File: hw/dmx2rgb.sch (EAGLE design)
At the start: 4 parts, among them IC1 ATMEGA88-20A

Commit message: basic schematics added new parts to library
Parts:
- added C1, C2, C3, C6, C7, C8: 100n, dmx2rgb:C0805
- added C10, C9: 100µ, dmx2rgb:CPOL-EUE2.5-7
- added C4, C5: (no value), dmx2rgb:C0805
- added IC2: 7805, dmx2rgb:78LXX
- added PAD1, PAD10, PAD11, PAD12, PAD13, PAD14, PAD15, PAD16, PAD2, PAD3, PAD4, PAD5, PAD6, PAD7, PAD8, PAD9: (no value), dmx2rgb:PAD_THT_1.6
- added Q1: (no value), dmx2rgb:CRYSTAL49
- added R1: 10k, dmx2rgb:R0805
- added R2, R3: (no value), dmx2rgb:R0805
- added U$10, U$4, U$5, U$6, U$7, U$8, U$9: IRF7303, dmx2rgb:IRF7303
- added U$3: SN75176B, dmx2rgb:SN75176B
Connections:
- new net +12V: C8.1, C9.+, IC2.IN
- new net +5V: C1.2, C10.+, C2.2, C3.1, C6.2, C7.1, IC1.AREF, IC1.AVCC, IC1.VCC@1, IC1.VCC@2, IC2.OUT, JP1.2, R1.2, U$2.VDD, U$3.VCC
- new net GND: C1.1, C10.-, C2.1, C3.2, C4.2, C5.2, C6.1, C7.2, C8.2, C9.-, IC1.AGND, IC1.GND@1, IC1.GND@2, IC2.GND, JP1.10, JP1.3, JP1.4, JP1.6, JP1.8, U$1.S1, U$1.S2, U$10.S1, U$10.S2, U$2.EXTCLK, U$2.VSS, U$3.GND, U$4.S1, U$4.S2, U$5.S1, U$5.S2, U$6.S1, U$6.S2, U$7.S1, U$7.S2, U$8.S1, U$8.S2, U$9.S1, U$9.S2
- new net N$1: IC1.(PCI16/RXD)PD0, U$3.R
- new net N$10: IC1.(PCI5/SCK)PB5, JP1.7
- new net N$11: U$3.B
- new net N$12: U$3.A
- new net N$13: PAD3.P, U$4.D1A, U$4.D1B
- new net N$14: PAD4.P, U$4.D2A, U$4.D2B
- new net N$16: U$2.LED4, U$4.G2
- new net N$17: PAD5.P, U$5.D1A, U$5.D1B
- new net N$18: PAD6.P, U$5.D2A, U$5.D2B
- new net N$19: U$2.LED3, U$5.G1
- new net N$2: IC1.(PCI17/TXD)PD1, U$3.D
- new net N$20: U$2.LED2, U$5.G2
- new net N$21: PAD7.P, U$6.D1A, U$6.D1B
- new net N$22: PAD8.P, U$6.D2A, U$6.D2B
- new net N$23: U$2.LED1, U$6.G1
- new net N$24: U$2.LED0, U$6.G2
- new net N$25: PAD9.P, U$7.D1A, U$7.D1B
- new net N$26: PAD10.P, U$7.D2A, U$7.D2B
- new net N$29: PAD11.P, U$8.D1A, U$8.D1B
- new net N$3: IC1.(PCI18/INT0)PD2, U$3.RE
- new net N$30: PAD12.P, U$8.D2A, U$8.D2B
- new net N$33: PAD13.P, U$9.D1A, U$9.D1B
- new net N$34: PAD14.P, U$9.D2A, U$9.D2B
- new net N$37: PAD15.P, U$10.D1A, U$10.D1B
- new net N$38: PAD16.P, U$10.D2A, U$10.D2B
- new net N$4: IC1.(PCI19/INT1/OC2B)PD3, U$3.DE
- new net N$41: C4.1, IC1.PB6(XTAL1/TOSC1/PCI6), Q1.1
- new net N$42: C5.1, IC1.PB7(XTAL2/TOSC2/PCI7), Q1.2
- new net N$5: PAD1.P, U$1.D1A, U$1.D1B
- new net N$50: U$1.G1, U$2.LED7
- new net N$51: U$1.G2, U$2.LED6
- new net N$52: U$2.LED5, U$4.G1
- new net N$53: U$2.LED8, U$7.G1
- new net N$54: U$2.LED9, U$7.G2
- new net N$55: U$2.LED10, U$8.G1
- new net N$56: U$2.LED11, U$8.G2
- new net N$57: U$2.LED12, U$9.G1
- new net N$58: U$2.LED13, U$9.G2
- new net N$59: U$10.G1, U$2.LED14
- new net N$6: PAD2.P, U$1.D2A, U$1.D2B
- new net N$60: U$10.G2, U$2.LED15
- new net N$7: IC1.PC6(/RESET/PCI14), JP1.5, R1.1
- new net N$8: IC1.(PCI3/MOSI/OC2A)PB3, JP1.1
- new net N$9: IC1.(PCI4/MISO)PB4, JP1.9
- new net SCL: IC1.(PCI13/ADC5/SCL)PC5, U$2.SCL
- new net SDA: IC1.(PCI12/ADC4/SDA)PC4, U$2.SDA
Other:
- moved on the sheet: JP1, U$1, U$2

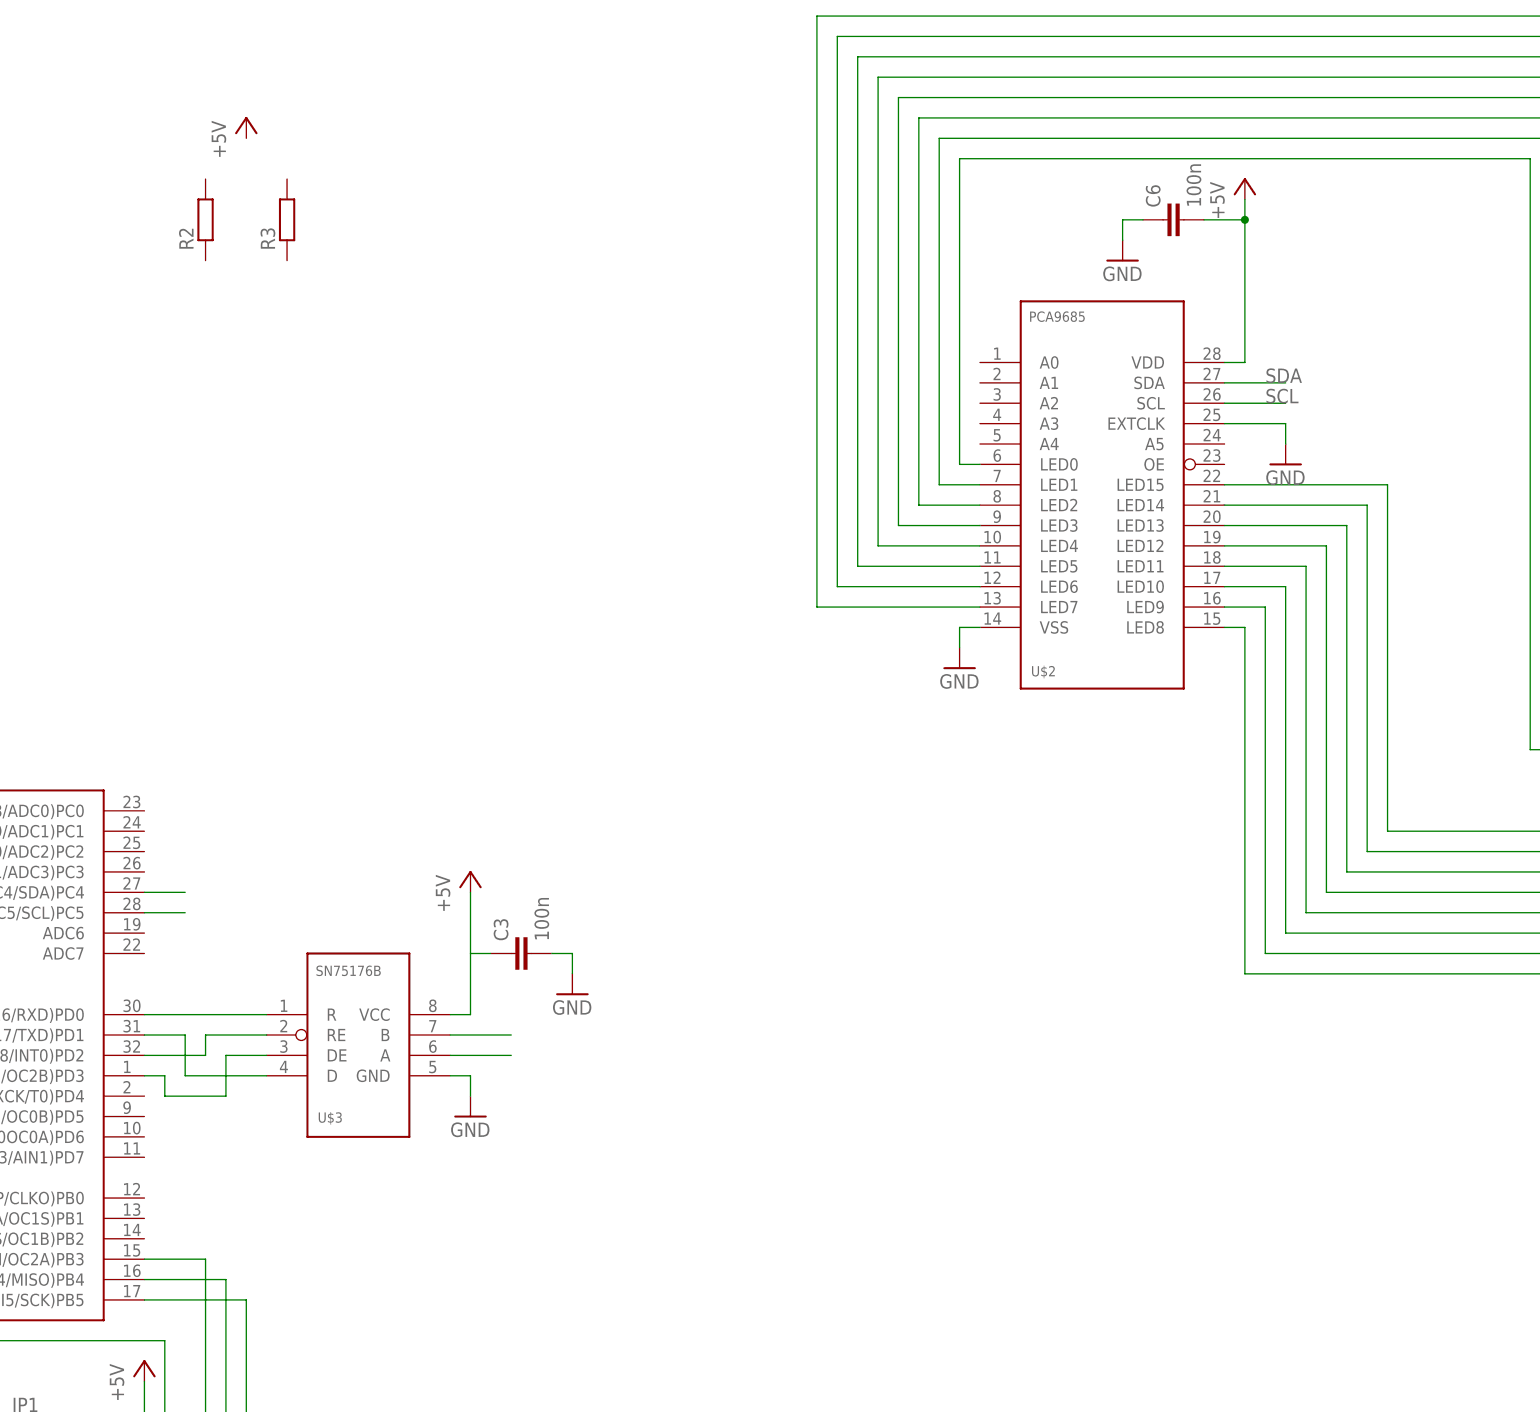
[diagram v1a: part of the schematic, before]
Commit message: added some pull ups added layout file
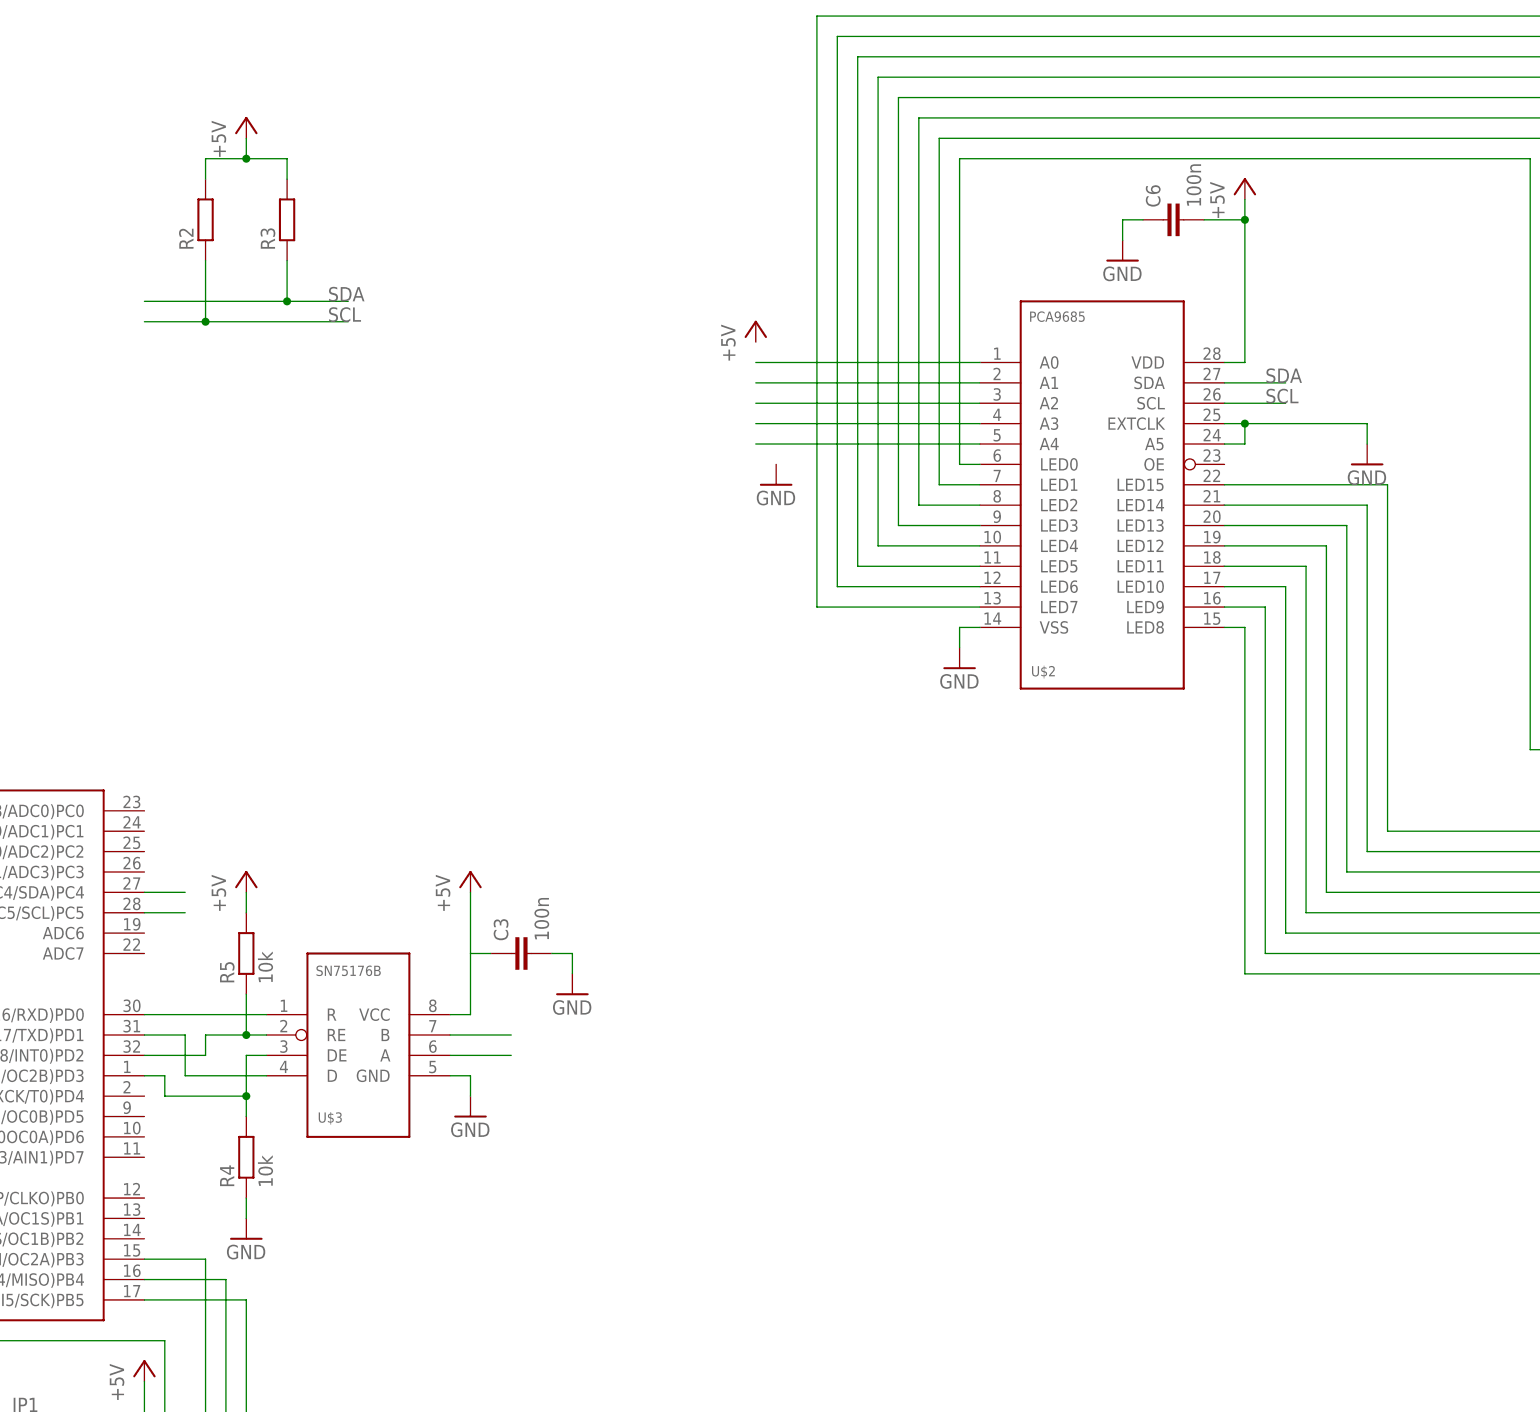
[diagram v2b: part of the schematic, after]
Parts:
- added R4, R5: 10k, dmx2rgb:R0805
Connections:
- new net N$15: U$2.A0
- new net N$27: U$2.A1
- new net N$28: U$2.A2
- new net N$31: U$2.A3
- new net N$32: U$2.A4
- net +5V: now also R2.2, R3.2, R5.2
- net GND: now also R4.1, U$2.A5
- net N$3: now also R5.1
- net N$4: now also R4.2
- net SCL: now also R2.1
- net SDA: now also R3.1
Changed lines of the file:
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@@
 <part name="R2" library="dmx2rgb" deviceset="R" device="0805"/>
 <part name="R3" library="dmx2rgb" deviceset="R" device="0805"/>
+<part name="R4" library="dmx2rgb" deviceset="R" device="0805" value="10k"/>
+<part name="R5" library="dmx2rgb" deviceset="R" device="0805" value="10k"/>
+<part name="P+10" library="dmx2rgb" deviceset="+5V" device=""/>
+<part name="GND20" library="dmx2rgb" deviceset="GND" device=""/>
+<part name="GND21" library="dmx2rgb" deviceset="GND" device=""/>
+<part name="P+11" library="dmx2rgb" deviceset="+5V" device=""/>
 </parts>
 <sheets>
@@
 <instance part="C6" gate="G$1" x="228.6" y="154.94" rot="R90"/>
 <instance part="GND16" gate="1" x="220.98" y="149.86"/>
-<instance part="GND17" gate="1" x="241.3" y="124.46"/>
+<instance part="GND17" gate="1" x="251.46" y="124.46"/>
 <instance part="GND18" gate="1" x="139.7" y="43.18"/>
 <instance part="IC2" gate="1" x="30.48" y="160.02"/>
@@
 <instance part="R2" gate="G$1" x="106.68" y="154.94" rot="R90"/>
 <instance part="R3" gate="G$1" x="116.84" y="154.94" rot="R90"/>
+<instance part="R4" gate="G$1" x="111.76" y="38.1" rot="R90"/>
+<instance part="R5" gate="G$1" x="111.76" y="63.5" rot="R90"/>
+<instance part="P+10" gate="1" x="111.76" y="73.66"/>
+<instance part="GND20" gate="1" x="111.76" y="27.94"/>
+<instance part="GND21" gate="1" x="177.8" y="121.92"/>
+<instance part="P+11" gate="1" x="175.26" y="142.24"/>
 </instances>
 <busses>
@@
 <segment>
 <pinref part="U$3" gate="G$1" pin="RE"/>
-<wire x1="114.3" y1="53.34" x2="106.68" y2="53.34" width="0.1524" layer="91"/>
+<wire x1="114.3" y1="53.34" x2="111.76" y2="53.34" width="0.1524" layer="91"/>
 <pinref part="IC1" gate="G$1" pin="(PCI18/INT0)PD2"/>
+<wire x1="111.76" y1="53.34" x2="106.68" y2="53.34" width="0.1524" layer="91"/>
 <wire x1="106.68" y1="53.34" x2="106.68" y2="50.8" width="0.1524" layer="91"/>
 <wire x1="106.68" y1="50.8" x2="99.06" y2="50.8" width="0.1524" layer="91"/>
+<pinref part="R5" gate="G$1" pin="1"/>
+<wire x1="111.76" y1="58.42" x2="111.76" y2="53.34" width="0.1524" layer="91"/>
+<junction x="111.76" y="53.34"/>
 </segment>
 </net>
@@
 <segment>
 <pinref part="U$3" gate="G$1" pin="DE"/>
-<wire x1="114.3" y1="50.8" x2="109.22" y2="50.8" width="0.1524" layer="91"/>
-<wire x1="109.22" y1="50.8" x2="109.22" y2="45.72" width="0.1524" layer="91"/>
-<wire x1="109.22" y1="45.72" x2="101.6" y2="45.72" width="0.1524" layer="91"/>
+<wire x1="114.3" y1="50.8" x2="111.76" y2="50.8" width="0.1524" layer="91"/>
+<wire x1="111.76" y1="50.8" x2="111.76" y2="45.72" width="0.1524" layer="91"/>
+<wire x1="111.76" y1="45.72" x2="101.6" y2="45.72" width="0.1524" layer="91"/>
 <wire x1="101.6" y1="45.72" x2="101.6" y2="48.26" width="0.1524" layer="91"/>
 <pinref part="IC1" gate="G$1" pin="(PCI19/INT1/OC2B)PD3"/>
 <wire x1="101.6" y1="48.26" x2="99.06" y2="48.26" width="0.1524" layer="91"/>
+<pinref part="R4" gate="G$1" pin="2"/>
+<wire x1="111.76" y1="45.72" x2="111.76" y2="43.18" width="0.1524" layer="91"/>
+<junction x="111.76" y="45.72"/>
 </segment>
 </net>
@@
 <junction x="40.64" y="160.02"/>
 <junction x="48.26" y="160.02"/>
+</segment>
+<segment>
+<pinref part="P+9" gate="1" pin="+5V"/>
+<wire x1="111.76" y1="165.1" x2="111.76" y2="162.56" width="0.1524" layer="91"/>
+<wire x1="111.76" y1="162.56" x2="106.68" y2="162.56" width="0.1524" layer="91"/>
+<pinref part="R2" gate="G$1" pin="2"/>
+<wire x1="106.68" y1="162.56" x2="106.68" y2="160.02" width="0.1524" layer="91"/>
+<pinref part="R3" gate="G$1" pin="2"/>
+<wire x1="111.76" y1="162.56" x2="116.84" y2="162.56" width="0.1524" layer="91"/>
+<wire x1="116.84" y1="162.56" x2="116.84" y2="160.02" width="0.1524" layer="91"/>
+<junction x="111.76" y="162.56"/>
+</segment>
+<segment>
+<pinref part="R5" gate="G$1" pin="2"/>
+<pinref part="P+10" gate="1" pin="+5V"/>
+<wire x1="111.76" y1="68.58" x2="111.76" y2="71.12" width="0.1524" layer="91"/>
 </segment>
 </net>
@@
 <segment>
 <pinref part="U$2" gate="G$1" pin="EXTCLK"/>
-<wire x1="233.68" y1="129.54" x2="241.3" y2="129.54" width="0.1524" layer="91"/>
-<wire x1="241.3" y1="129.54" x2="241.3" y2="127" width="0.1524" layer="91"/>
+<wire x1="233.68" y1="129.54" x2="236.22" y2="129.54" width="0.1524" layer="91"/>
+<wire x1="236.22" y1="129.54" x2="251.46" y2="129.54" width="0.1524" layer="91"/>
+<wire x1="251.46" y1="129.54" x2="251.46" y2="127" width="0.1524" layer="91"/>
 <pinref part="GND17" gate="1" pin="GND"/>
+<pinref part="U$2" gate="G$1" pin="A5"/>
+<wire x1="233.68" y1="127" x2="236.22" y2="127" width="0.1524" layer="91"/>
+<wire x1="236.22" y1="127" x2="236.22" y2="129.54" width="0.1524" layer="91"/>
+<junction x="236.22" y="129.54"/>
 </segment>
 <segment>
@@
 <junction x="20.32" y="147.32"/>
 </segment>
+<segment>
+<pinref part="R4" gate="G$1" pin="1"/>
+<pinref part="GND20" gate="1" pin="GND"/>
+<wire x1="111.76" y1="33.02" x2="111.76" y2="30.48" width="0.1524" layer="91"/>
+</segment>
 </net>
 <net name="N$7" class="0">
@@
 <wire x1="99.06" y1="71.12" x2="104.14" y2="71.12" width="0.1524" layer="91"/>
 </segment>
+<segment>
+<wire x1="99.06" y1="144.78" x2="116.84" y2="144.78" width="0.1524" layer="91"/>
+<pinref part="R3" gate="G$1" pin="1"/>
+<wire x1="116.84" y1="144.78" x2="124.46" y2="144.78" width="0.1524" layer="91"/>
+<wire x1="116.84" y1="149.86" x2="116.84" y2="144.78" width="0.1524" layer="91"/>
+<junction x="116.84" y="144.78"/>
+<label x="121.92" y="144.78" size="1.778" layer="95"/>
+</segment>
 </net>
 <net name="SCL" class="0">
@@
 <pinref part="IC1" gate="G$1" pin="(PCI13/ADC5/SCL)PC5"/>
 <wire x1="99.06" y1="68.58" x2="104.14" y2="68.58" width="0.1524" layer="91"/>
+</segment>
+<segment>
+<wire x1="99.06" y1="142.24" x2="106.68" y2="142.24" width="0.1524" layer="91"/>
+<pinref part="R2" gate="G$1" pin="1"/>
+<wire x1="106.68" y1="142.24" x2="124.46" y2="142.24" width="0.1524" layer="91"/>
+<wire x1="106.68" y1="149.86" x2="106.68" y2="142.24" width="0.1524" layer="91"/>
+<junction x="106.68" y="142.24"/>
+<label x="121.92" y="142.24" size="1.778" layer="95"/>
 </segment>
 </net>
@@
 </segment>
 </net>
+<net name="N$15" class="0">
+<segment>
+<pinref part="U$2" gate="G$1" pin="A0"/>
+<wire x1="203.2" y1="137.16" x2="175.26" y2="137.16" width="0.1524" layer="91"/>
+</segment>
+</net>
+<net name="N$27" class="0">
+<segment>
+<pinref part="U$2" gate="G$1" pin="A1"/>
+<wire x1="203.2" y1="134.62" x2="175.26" y2="134.62" width="0.1524" layer="91"/>
+</segment>
+</net>
+<net name="N$28" class="0">
+<segment>
+<pinref part="U$2" gate="G$1" pin="A2"/>
+<wire x1="203.2" y1="132.08" x2="175.26" y2="132.08" width="0.1524" layer="91"/>
+</segment>
+</net>
+<net name="N$31" class="0">
+<segment>
+<pinref part="U$2" gate="G$1" pin="A3"/>
+<wire x1="203.2" y1="129.54" x2="175.26" y2="129.54" width="0.1524" layer="91"/>
+</segment>
+</net>
+<net name="N$32" class="0">
+<segment>
+<pinref part="U$2" gate="G$1" pin="A4"/>
+<wire x1="203.2" y1="127" x2="175.26" y2="127" width="0.1524" layer="91"/>
+</segment>
+</net>
